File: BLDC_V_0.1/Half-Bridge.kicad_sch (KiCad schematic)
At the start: 11 parts, among them J5 Screw_Terminal_01x01, Q1 NMOS, Q2 NMOS, U4 AD8418A

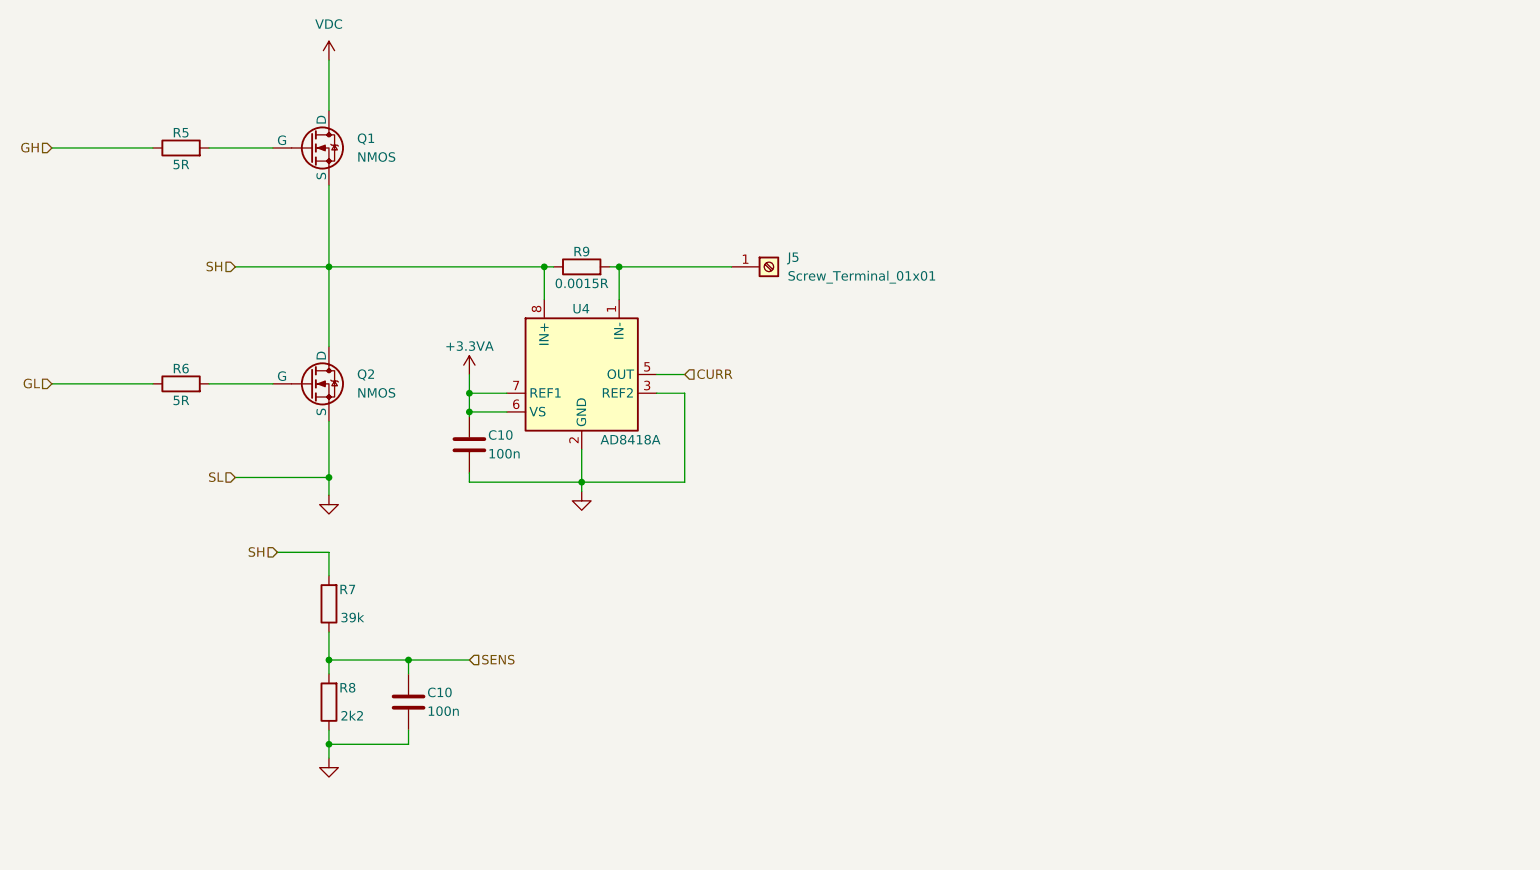
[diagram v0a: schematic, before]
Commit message: Connectors and CAN circuit added.
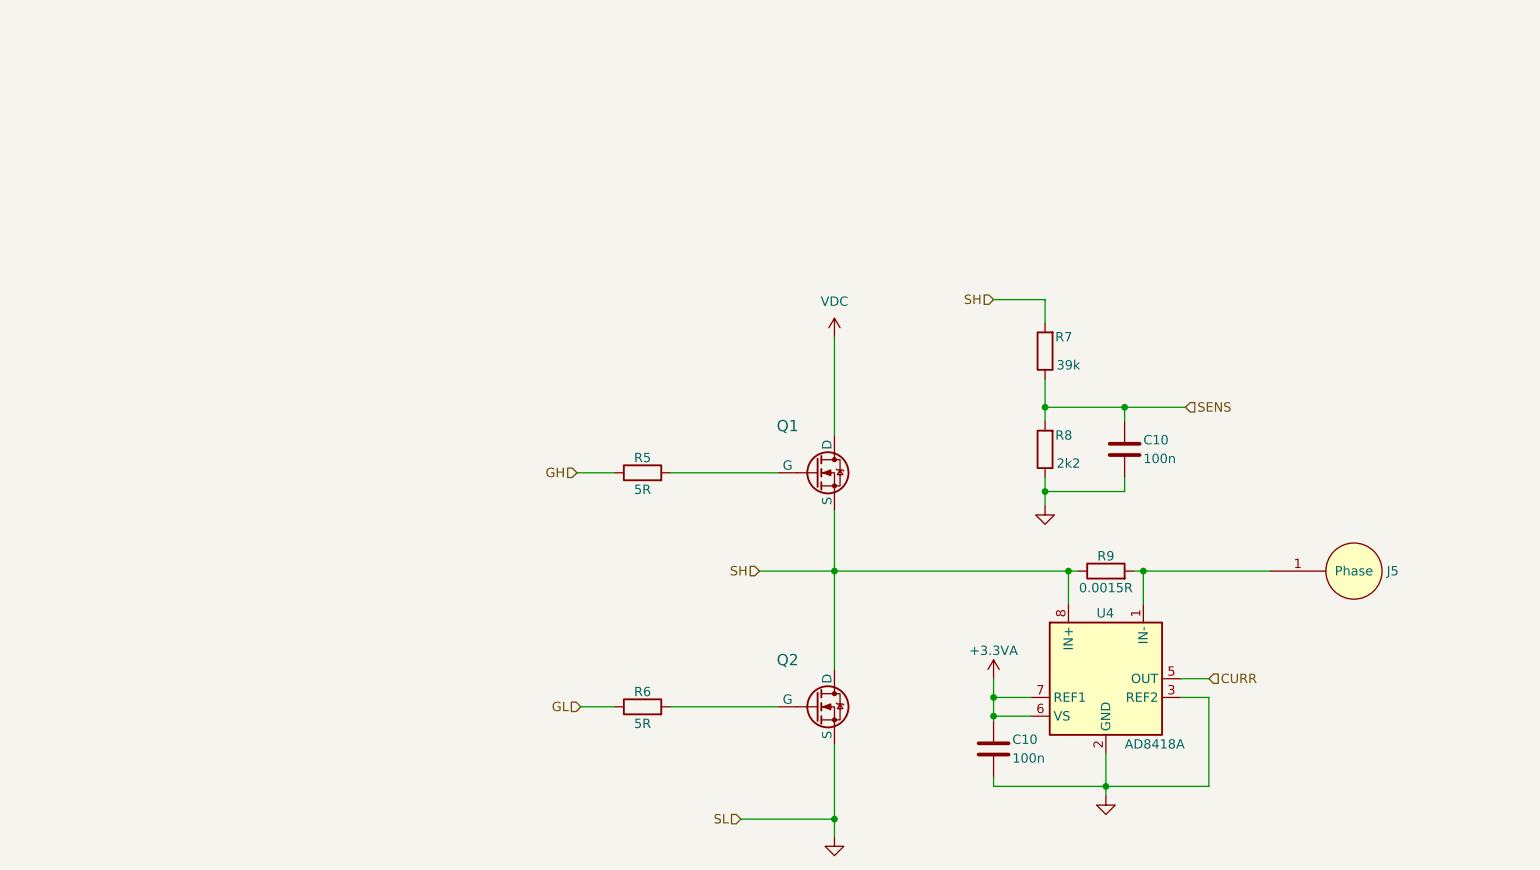
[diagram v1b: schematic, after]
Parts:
- removed J5: Screw_Terminal_01x01, symbol Connector:Screw_Terminal_01x01
- added J5: Phase, Connector:Power_Welding_Pad_10x10mm, symbol Connector_Generic:Power_Welding_PAD
- Q1, Q2: value NMOS -> BSC070N10NS5SCATMA1; footprint (none) -> BSC070N:PG-WSON-8
- U4: footprint (none) -> Package_SO:SOIC-8_3.9x4.9mm_P1.27mm; Link (none) -> https://jlcpcb.com/partdetail/AnalogDevices-AD8418AWBRZRL/C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
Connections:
- net at R9.2, U4.1 (IN-): now also J5.1
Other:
- moved on the sheet: C10, Q1, R5, R6, R7, R8, R9, U4

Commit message: Schematic prototip done.
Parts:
- C10: footprint (none) -> Capacitor_SMD:C_0402_1005Metric
- R5, R6: footprint (none) -> Resistor_SMD:R_0805_2012Metric
- R7, R8: footprint (none) -> Resistor_SMD:R_0603_1608Metric
- R9: footprint (none) -> Resistor_SMD:R_2512_6332Metric; Comment (none) -> 3W; Link (none) -> https://jlcpcb.com/partdetail/Milliohm-LR2512D_3W_1_5mR_1/C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
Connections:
- net GND: now also Q2.S; no longer Q2.3 (S)
- net SH: now also Q1.S, Q2.D; no longer Q1.3 (S), Q2.1 (D)
- net VDC: now also Q1.D; no longer Q1.1 (D)
- net at R6.2: now also Q2.G; no longer Q2.2 (G)
- net at R5.2: now also Q1.G; no longer Q1.2 (G)
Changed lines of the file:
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@@
       (effects (font (size 1.27 1.27)) (justify left))
     )
-    (property "Footprint" "" (at 169.8752 79.375 0)
+    (property "Footprint" "Capacitor_SMD:C_0402_1005Metric" (at 169.8752 79.375 0)
       (effects (font (size 1.27 1.27)) hide)
     )
@@
       (effects (font (size 1.27 1.27)))
     )
-    (property "Footprint" "" (at 159.893 62.23 90)
+    (property "Footprint" "Resistor_SMD:R_0603_1608Metric" (at 159.893 62.23 90)
       (effects (font (size 1.27 1.27)) hide)
     )
@@
       (effects (font (size 1.27 1.27)) hide)
     )
-    (pin "1")
-    (pin "2")
-    (pin "3")
+    (pin "D")
+    (pin "G")
+    (pin "S")
     (instances
       (project "BLDC_V_0.1"
@@
       (effects (font (size 1.27 1.27)))
     )
-    (property "Footprint" "" (at 166.37 93.853 90)
+    (property "Footprint" "Resistor_SMD:R_2512_6332Metric" (at 166.37 93.853 90)
       (effects (font (size 1.27 1.27)) hide)
     )
@@
       (effects (font (size 1.27 1.27)) hide)
     )
-    (property "Comment" "" (at 166.37 92.075 90)
+    (property "Link" "https://jlcpcb.com/partdetail/Milliohm-LR2512D_3W_1_5mR_1/C500735" (at 166.37 92.075 90)
+      (effects (font (size 1.27 1.27)) hide)
+    )
+    (property "Comment" "3W" (at 166.37 92.075 90)
       (effects (font (size 1.27 1.27)) hide)
     )
@@
       (effects (font (size 1.27 1.27)))
     )
-    (property "Footprint" "" (at 103.505 80.518 90)
+    (property "Footprint" "Resistor_SMD:R_0805_2012Metric" (at 103.505 80.518 90)
       (effects (font (size 1.27 1.27)) hide)
     )
@@
       (effects (font (size 1.27 1.27)) hide)
     )
-    (pin "1")
-    (pin "2")
-    (pin "3")
+    (pin "D")
+    (pin "G")
+    (pin "S")
     (instances
       (project "BLDC_V_0.1"
@@
       (effects (font (size 1.27 1.27)))
     )
-    (property "Footprint" "" (at 103.505 112.268 90)
+    (property "Footprint" "Resistor_SMD:R_0805_2012Metric" (at 103.505 112.268 90)
       (effects (font (size 1.27 1.27)) hide)
     )
@@
       (effects (font (size 1.27 1.27)))
     )
-    (property "Footprint" "" (at 159.893 75.565 90)
+    (property "Footprint" "Resistor_SMD:R_0603_1608Metric" (at 159.893 75.565 90)
       (effects (font (size 1.27 1.27)) hide)
     )
@@
       (effects (font (size 1.27 1.27)) (justify left))
     )
-    (property "Footprint" "" (at 152.0952 120.015 0)
-      (effects (font (size 1.27 1.27)) hide)
-    )
+    (property "Footprint" "Capacitor_SMD:C_0402_1005Metric" (at 152.0952 120.015 0)
+      (effects (font (size 1.27 1.27)) hide)
+    )

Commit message: PCB placement completed.
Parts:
- added C57: 1u, Capacitor_SMD:C_1206_3216Metric, symbol Device:C
- added C60: 330n, Capacitor_SMD:C_0805_2012Metric, symbol Device:C
- added C63: 15n, Capacitor_SMD:C_0603_1608Metric, symbol Device:C
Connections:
- net GND: now also C57.2, C60.2, C63.2
- net VDC: now also C57.1, C60.1, C63.1
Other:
- moved on the sheet: C10, J5, R7, R8, R9, U4
